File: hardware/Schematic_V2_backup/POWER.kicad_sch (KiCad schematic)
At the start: 50 parts, among them J3 Screw_Terminal_01x03, U11 TPS5430DDA, U4 AMS1117-3.3, U7 TPS5430DDA

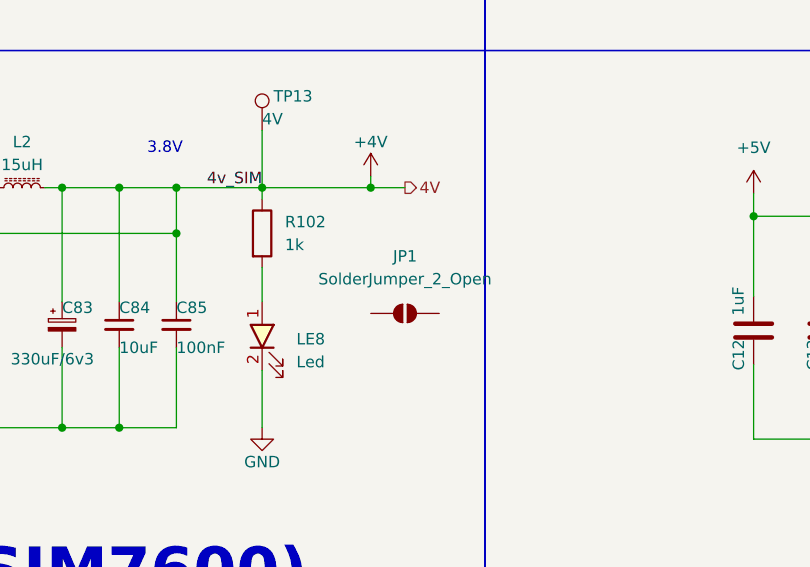
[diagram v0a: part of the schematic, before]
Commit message: Update PCB Layout for Gateway, 23/3/2026
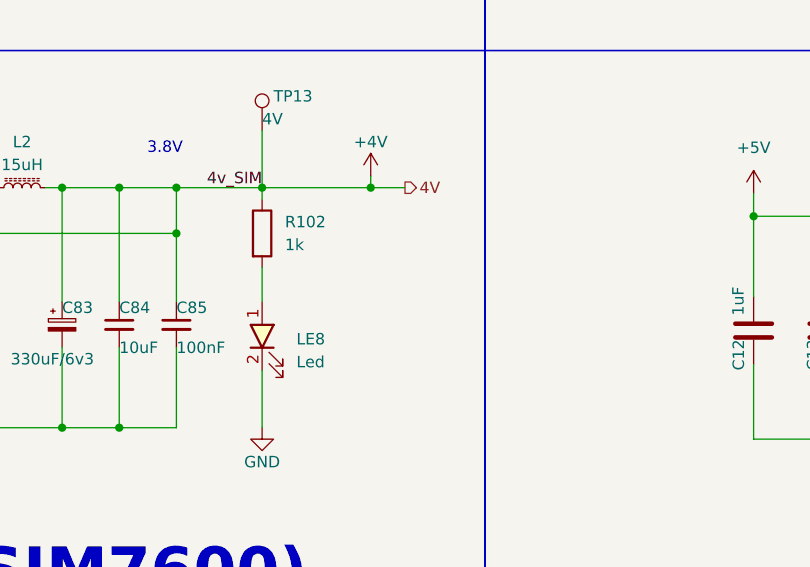
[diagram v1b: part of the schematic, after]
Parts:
- removed JP1: SolderJumper_2_Open, symbol Jumper:SolderJumper_2_Open
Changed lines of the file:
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@@
-	)
-	(symbol
-		(lib_id "Jumper:SolderJumper_2_Open")
-		(at 154.94 124.46 0)
-		(unit 1)
-		(exclude_from_sim yes)
-		(in_bom no)
-		(on_board yes)
-		(dnp no)
-		(fields_autoplaced yes)
-		(property "Reference" "JP1"
-			(at 154.94 118.11 0)
-			(effects
-				(font
-					(size 1.27 1.27)
-				)
-			)
-		)
-		(property "Value" "SolderJumper_2_Open"
-			(at 154.94 120.65 0)
-			(effects
-				(font
-					(size 1.27 1.27)
-				)
-			)
-		)
-		(property "Footprint" ""
-			(at 154.94 124.46 0)
-			(effects
-				(font
-					(size 1.27 1.27)
-				)
-				(hide yes)
-			)
-		)
-		(property "Datasheet" "~"
-			(at 154.94 124.46 0)
-			(effects
-				(font
-					(size 1.27 1.27)
-				)
-				(hide yes)
-			)
-		)
-		(property "Description" "Solder Jumper, 2-pole, open"
-			(at 154.94 124.46 0)
-			(effects
-				(font
-					(size 1.27 1.27)
-				)
-				(hide yes)
-			)
-		)
-		(pin "2"
-		)
-		(pin "1"
-		)
-		(instances
-			(project ""
-				(path "/08b065f5-231d-43cb-bb9e-87dca43beac9/be7dc874-3a80-4125-bbf4-83e9b6dc8646"
-					(reference "JP1")
-					(unit 1)
-				)
-			)
-		)
 	)
 	(symbol
